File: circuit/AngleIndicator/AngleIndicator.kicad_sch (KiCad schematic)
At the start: 0 parts

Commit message: initial commit
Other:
- title: Template -> AngleIndicator
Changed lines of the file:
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@@
 	(paper "A4")
 	(title_block
-		(title "Template")
+		(title "AngleIndicator")
 		(rev "0.0")
 		(company "AIOLIA")

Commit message: 回路図&PCB追加
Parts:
- added C1, C2, C3, C4, C6: 0.1u, Capacitor_SMD:C_0603_1608Metric_Pad1.08x0.95mm_HandSolder, symbol Device:C
- added C5: 1.0u, Capacitor_SMD:C_0603_1608Metric_Pad1.08x0.95mm_HandSolder, symbol Device:C
- added D1: LED, Diode_SMD:D_0603_1608Metric_Pad1.05x0.95mm_HandSolder, symbol Device:LED
- added J1: Conn_01x06, Connector_JST:JST_ZH_B6B-ZR_1x06_P1.50mm_Vertical, symbol Connector_Generic:Conn_01x06
- added J2: Conn_01x04, Connector_JST:JST_PH_B4B-PH-SM4-TB_1x04-1MP_P2.00mm_Vertical, symbol Connector_Generic:Conn_01x04
- added R2, R3, R4: 100, Resistor_SMD:R_0603_1608Metric_Pad0.98x0.95mm_HandSolder, symbol Device:R
- added R5: 120, Resistor_SMD:R_0603_1608Metric_Pad0.98x0.95mm_HandSolder, symbol Device:R
- added U1: ~, AIOLIA:SOT95P280X130-5N, symbol AIOLIA:NJM2866F33
- added U2: STM32G441KBTx, Package_QFP:LQFP-32_7x7mm_P0.8mm, symbol MCU_ST_STM32G4:STM32G441KBTx
- added U3: ~, Package_TO_SOT_SMD:SOT-23-8_Handsoldering, symbol AIOLIA:TCAN3413DDR
- added U4: ~, Package_SO:SOIC-8_3.9x4.9mm_P1.27mm, symbol AIOLIA:AS5600
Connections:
- new net: D1.1 (K), R2.2
- new net +3V3: C3.1, C4.1, C5.2, C6.1, J1.5 (Pin_5), R3.2, U1.5 (Vout), U2.1 (VDD), U2.15 (VDDA), U2.17 (VDD), U3.3 (VCC), U3.5 (VIO), U4.1 (VDD5V), U4.2 (VDD3V3)
- new net BOOT0: R3.1, R4.2, U2.31 (PB8)
- new net CAN+: J2.1 (Pin_1), R5.2, U3.7 (CANH)
- new net CAN-: J2.2 (Pin_2), R5.1, U3.6 (CANL)
- new net CAN_RX: U2.21 (PA11), U3.4 (RXD)
- new net CAN_TX: U2.22 (PA12), U3.1 (TXD)
- new net GND: C1.2, C2.2, C3.2, C4.2, C5.1, C6.2, J1.6 (Pin_6), J2.3 (Pin_3), R2.1, R4.1, U1.2 (GND), U2.14 (VSSA), U2.16 (VSS), U2.32 (VSS), U3.2 (GND), U3.8 (STB), U4.4 (GND)
- new net LED1: D1.2 (A), U2.18 (PA8)
- new net RST: C1.1, U2.4 (PG10)
- new net RX2: J1.1 (Pin_1), U2.8 (PA3)
- new net SCL: U2.25 (PA15), U4.7 (SCL)
- new net SDA: U2.30 (PB7), U4.6 (SDA)
- new net SWCLK: J1.4 (Pin_4), U2.24 (PA14)
- new net SWDIO: J1.3 (Pin_3), U2.23 (PA13)
- new net TX2: J1.2 (Pin_2), U2.7 (PA2)
- new net VCC: C2.1, J2.4 (Pin_4), U1.1 (Vin), U1.3 (CONTROL)
- no-connect marks 0 -> 18

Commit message: 1/09発注分
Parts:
- J2: footprint Connector_JST:JST_PH_B4B-PH-SM4-TB_1x04-1MP_P2.00mm_Vertical -> Connector_JST:JST_PH_S4B-PH-K_1x04_P2.00mm_Horizontal
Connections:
- net DIR: now reaches U4.8 (DIR)
- net DIR: now also U2.26 (PB3)
- no-connect marks 18 -> 16
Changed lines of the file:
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@@
-	)
-	(no_connect
-		(at 114.3 58.42)
 	)
 	(no_connect
@@
 	(no_connect
 		(at 139.7 43.18)
-	)
-	(no_connect
-		(at 116.84 111.76)
 	)
 	(no_connect
@@
 	)
 	(global_label "CAN_RX"
-		(shape input)
+		(shape output)
 		(at 167.64 69.85 180)
 		(fields_autoplaced yes)
@@
 		)
 	)
+	(global_label "DIR"
+		(shape output)
+		(at 114.3 58.42 180)
+		(fields_autoplaced yes)
+		(effects
+			(font
+				(size 1.27 1.27)
+			)
+			(justify right)
+		)
+		(property "Intersheetrefs" "${INTERSHEET_REFS}"
+			(at 108.17 58.42 0)
+			(effects
+				(font
+					(size 1.27 1.27)
+				)
+				(justify right)
+				(hide yes)
+			)
+		)
+	)
 	(global_label "RST"
-		(shape input)
+		(shape output)
 		(at 36.83 36.83 0)
 		(fields_autoplaced yes)
@@
 	)
 	(global_label "SDA"
-		(shape input)
+		(shape bidirectional)
 		(at 116.84 121.92 0)
 		(fields_autoplaced yes)
@@
 		)
 		(property "Intersheetrefs" "${INTERSHEET_REFS}"
-			(at 123.3933 121.92 0)
+			(at 124.5046 121.92 0)
 			(effects
 				(font
@@
 	)
 	(global_label "RX2"
-		(shape input)
+		(shape output)
 		(at 195.58 29.21 180)
 		(fields_autoplaced yes)
@@
 	)
 	(global_label "CAN_TX"
-		(shape input)
+		(shape output)
 		(at 139.7 73.66 0)
 		(fields_autoplaced yes)
@@
 	)
 	(global_label "SWCLK"
+		(shape output)
+		(at 195.58 36.83 180)
+		(fields_autoplaced yes)
+		(effects
+			(font
+				(size 1.27 1.27)
+			)
+			(justify right)
+		)
+		(property "Intersheetrefs" "${INTERSHEET_REFS}"
+			(at 186.3658 36.83 0)
+			(effects
+				(font
+					(size 1.27 1.27)
+				)
+				(justify right)
+				(hide yes)
+			)
+		)
+	)
+	(global_label "DIR"
 		(shape input)
-		(at 195.58 36.83 180)
-		(fields_autoplaced yes)
-		(effects
-			(font
-				(size 1.27 1.27)
-			)
-			(justify right)
-		)
-		(property "Intersheetrefs" "${INTERSHEET_REFS}"
-			(at 186.3658 36.83 0)
-			(effects
-				(font
-					(size 1.27 1.27)
-				)
-				(justify right)
+		(at 116.84 111.76 0)
+		(fields_autoplaced yes)
+		(effects
+			(font
+				(size 1.27 1.27)
+			)
+			(justify left)
+		)
+		(property "Intersheetrefs" "${INTERSHEET_REFS}"
+			(at 122.97 111.76 0)
+			(effects
+				(font
+					(size 1.27 1.27)
+				)
+				(justify left)
 				(hide yes)
 			)
@@
 	)
 	(global_label "SDA"
-		(shape input)
+		(shape bidirectional)
 		(at 114.3 68.58 180)
 		(fields_autoplaced yes)
@@
 		)
 		(property "Intersheetrefs" "${INTERSHEET_REFS}"
-			(at 107.7467 68.58 0)
+			(at 106.6354 68.58 0)
 			(effects
 				(font
@@
 	)
 	(global_label "LED1"
-		(shape input)
+		(shape output)
 		(at 139.7 63.5 0)
 		(fields_autoplaced yes)
@@
 	)
 	(global_label "SWDIO"
-		(shape input)
+		(shape bidirectional)
 		(at 139.7 76.2 0)
 		(fields_autoplaced yes)
@@
 		)
 		(property "Intersheetrefs" "${INTERSHEET_REFS}"
-			(at 148.5514 76.2 0)
+			(at 149.6627 76.2 0)
 			(effects
 				(font
@@
 	)
 	(global_label "SWDIO"
-		(shape input)
+		(shape bidirectional)
 		(at 195.58 34.29 180)
 		(fields_autoplaced yes)
@@
 		)
 		(property "Intersheetrefs" "${INTERSHEET_REFS}"
-			(at 186.7286 34.29 0)
+			(at 185.6173 34.29 0)
 			(effects
 				(font
@@
 	)
 	(global_label "TX2"
-		(shape input)
+		(shape output)
 		(at 139.7 48.26 0)
 		(fields_autoplaced yes)
@@
 	)
 	(global_label "SCL"
-		(shape input)
+		(shape output)
 		(at 139.7 81.28 0)
 		(fields_autoplaced yes)
@@
 			)
 		)
-		(property "Footprint" "Connector_JST:JST_PH_B4B-PH-SM4-TB_1x04-1MP_P2.00mm_Vertical"
+		(property "Footprint" "Connector_JST:JST_PH_S4B-PH-K_1x04_P2.00mm_Horizontal"
 			(at 219.71 73.66 0)
 			(effects

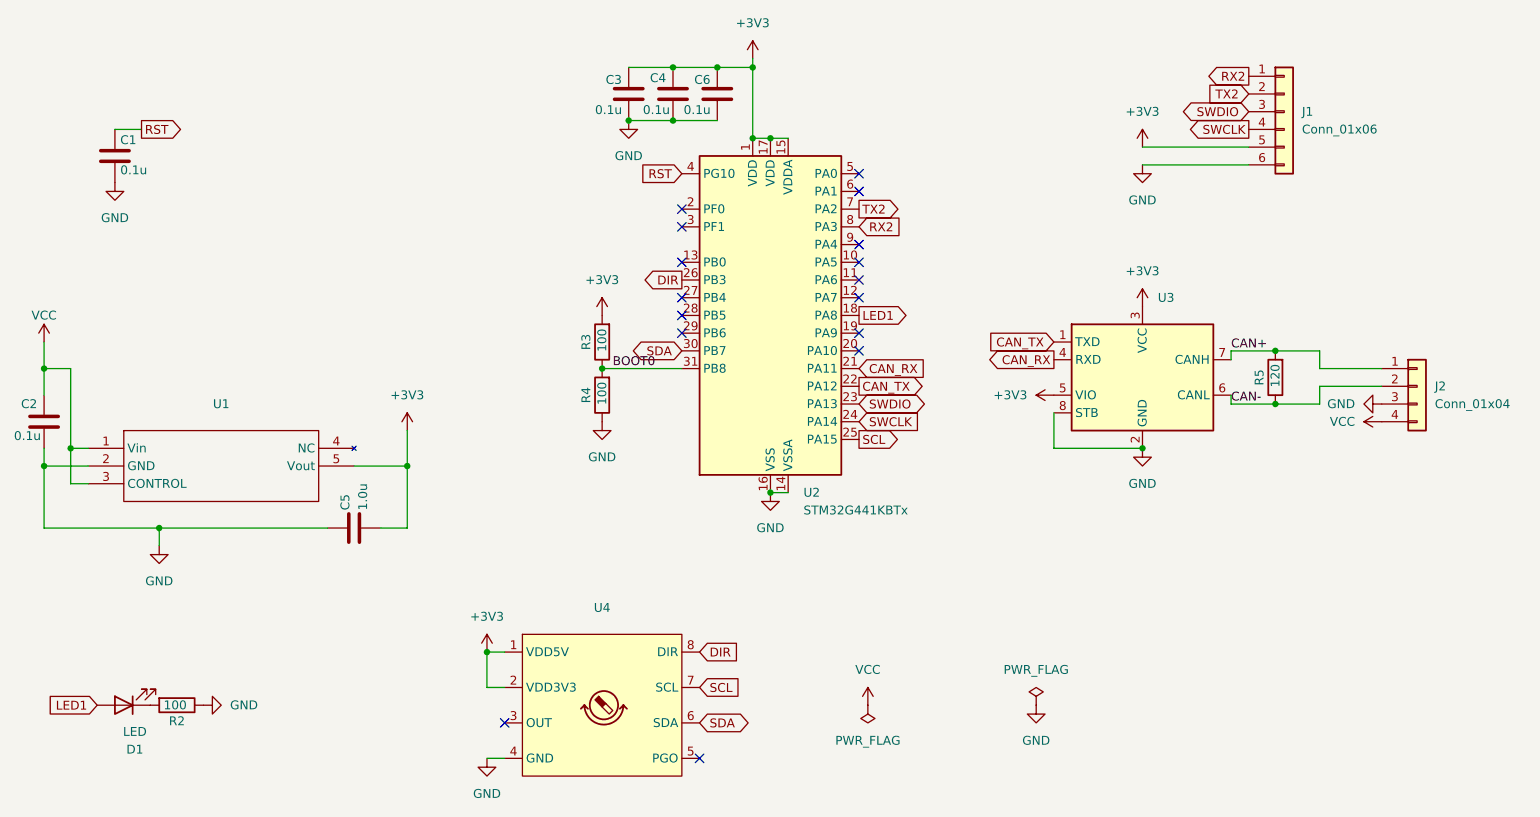
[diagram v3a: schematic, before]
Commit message: pull-up抵抗とアナログ入力を追加
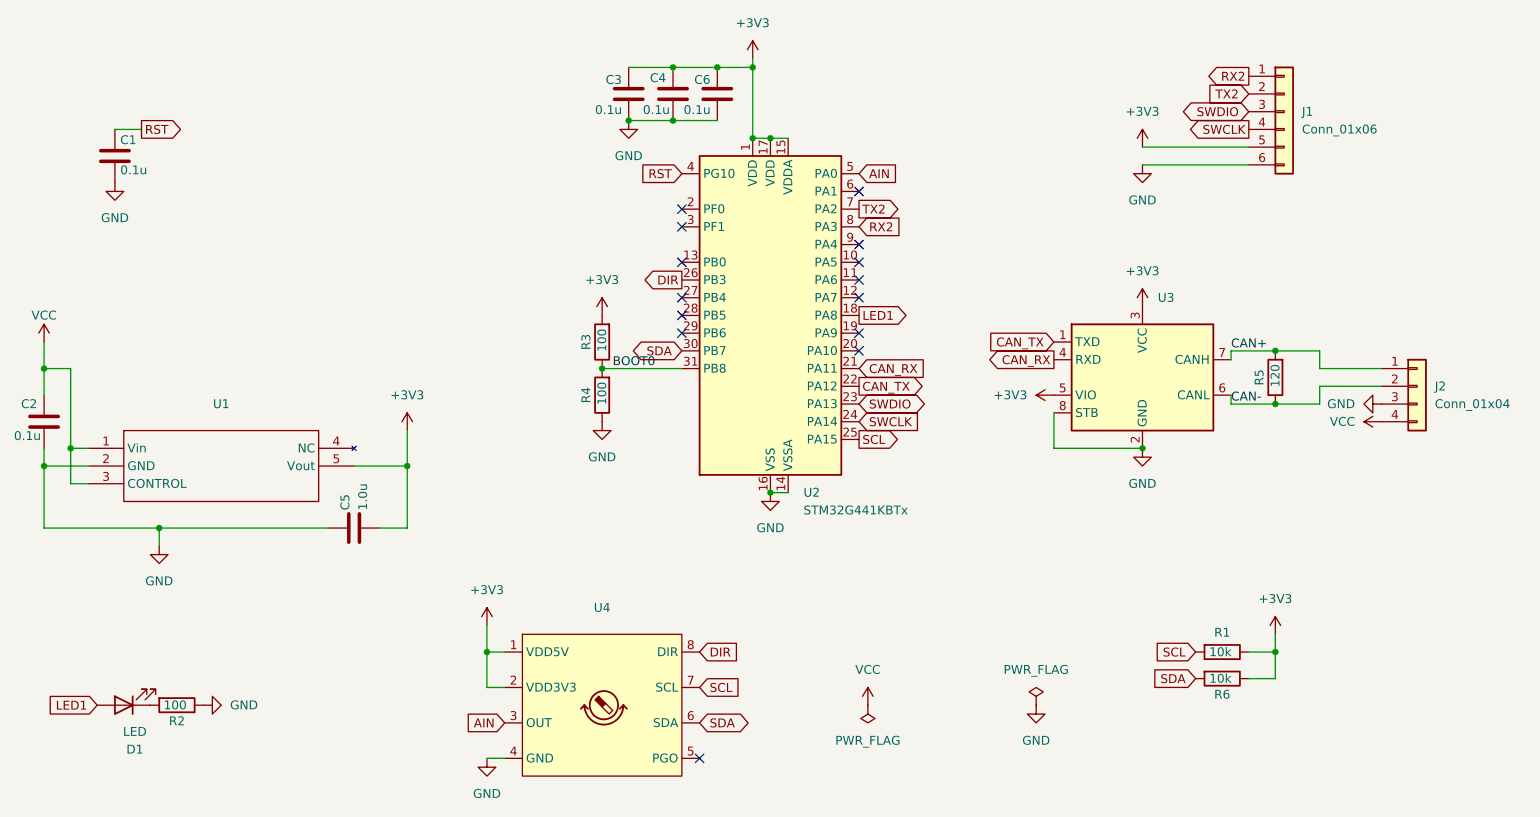
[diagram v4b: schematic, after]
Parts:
- added R1, R6: 10k, Resistor_SMD:R_0603_1608Metric_Pad0.98x0.95mm_HandSolder, symbol Device:R
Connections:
- net +3V3: now also R1.1, R6.1
- net SCL: now also R1.2
- net SDA: now also R6.2
- net AIN: now reaches U4.3 (OUT)
- net AIN: now also U2.5 (PA0)
- no-connect marks 16 -> 14

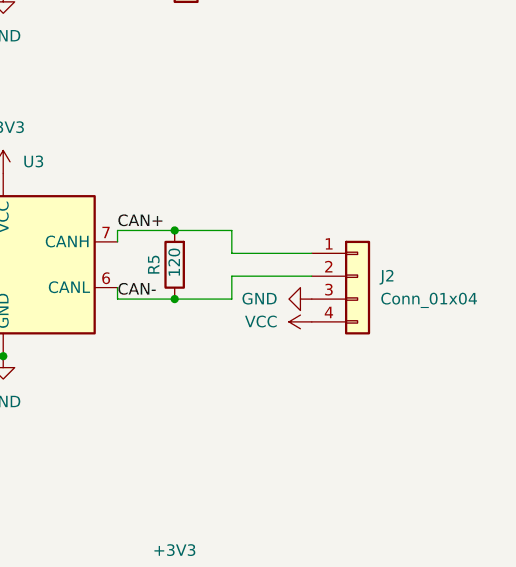
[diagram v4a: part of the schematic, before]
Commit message: CANコネクタの配置を変更
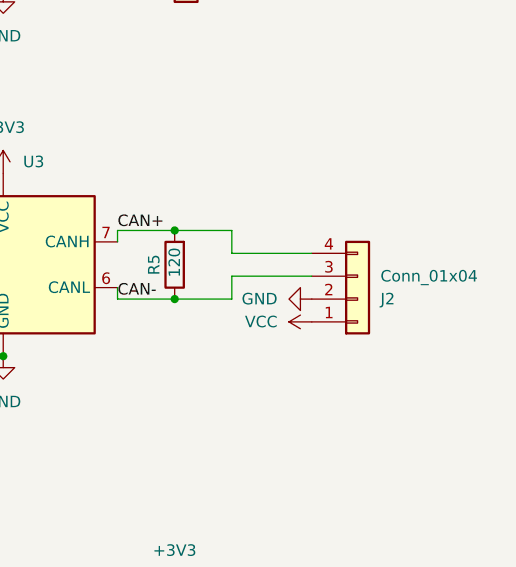
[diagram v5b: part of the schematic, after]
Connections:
- net CAN+: now also J2.4 (Pin_4); no longer J2.1 (Pin_1)
- net CAN-: now also J2.3 (Pin_3); no longer J2.2 (Pin_2)
- net GND: now also J2.2 (Pin_2); no longer J2.3 (Pin_3)
- net VCC: now also J2.1 (Pin_1); no longer J2.4 (Pin_4)
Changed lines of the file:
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@@
 	(symbol
 		(lib_id "Connector_Generic:Conn_01x04")
-		(at 219.71 73.66 0)
+		(at 219.71 76.2 0)
+		(mirror x)
 		(unit 1)
 		(exclude_from_sim no)
@@
 		(dnp no)
 		(property "Reference" "J2"
-			(at 222.25 73.6599 0)
+			(at 222.25 76.2001 0)
 			(effects
 				(font
@@
 		)
 		(property "Value" "Conn_01x04"
-			(at 222.25 76.1999 0)
+			(at 222.25 73.6601 0)
 			(effects
 				(font
@@
 		)
 		(property "Footprint" "Connector_JST:JST_PH_S4B-PH-K_1x04_P2.00mm_Horizontal"
-			(at 219.71 73.66 0)
+			(at 219.71 76.2 0)
 			(effects
 				(font
@@
 		)
 		(property "Datasheet" "~"
-			(at 219.71 73.66 0)
+			(at 219.71 76.2 0)
 			(effects
 				(font
@@
 		)
 		(property "Description" "Generic connector, single row, 01x04, script generated (kicad-library-utils/schlib/autogen/connector/)"
-			(at 219.71 73.66 0)
+			(at 219.71 76.2 0)
 			(effects
 				(font
